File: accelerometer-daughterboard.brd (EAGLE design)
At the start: 3.7 x 11.9 mm, 4 parts, among them U1 LIS3DHTR

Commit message: Tweak
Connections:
- net INT1: now also U$1.P$4
- net SAO: no longer U$1.P$4
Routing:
- net SAO: track 1.59 -> 0.00 mm, vias 1 -> 0
- net INT1: track 0.00 -> 1.57 mm, vias 0 -> 1
- net 3.3V: track 15.7 -> 16.6 mm
- net GND: track 12.9 -> 13.4 mm
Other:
- board text added: "INT1"
- board text removed: "SAO"
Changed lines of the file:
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@@
 <wire x1="9.555834375" y1="16.78234375" x2="8.539834375" y2="17.79834375" width="0.254" layer="21" curve="-90"/>
 <wire x1="8.539834375" y1="17.79834375" x2="9.555834375" y2="18.81434375" width="0.254" layer="21" curve="-92"/>
-<text x="8.81850625" y="13.959309375" size="1.016" layer="22" font="vector" ratio="14" rot="MR0" align="center">SAO</text>
+<text x="8.81850625" y="13.959309375" size="1.016" layer="22" font="vector" ratio="14" rot="MR0" align="center">INT1</text>
 <dimension x1="10.760978125" y1="21.208690625" x2="10.75999375" y2="9.27154375" x3="13.9503125" y3="15.239853125" textsize="1.778" layer="47"/>
 <dimension x1="7.021409375" y1="9.268590625" x2="10.7619625" y2="9.26760625" x3="8.890953125" y3="6.496278125" textsize="1.778" layer="47"/>
@@
 <wire x1="9.1202" y1="12.45" x2="9.1202" y2="12.21" width="0.254" layer="1"/>
 <wire x1="9.1202" y1="12.21" x2="9.4" y2="11.9302" width="0.254" layer="1"/>
-<wire x1="9.0984" y1="12.40656875" x2="8.39" y2="11.69816875" width="0.254" layer="1"/>
 <wire x1="9.1202" y1="12.45" x2="9.0984" y2="12.4282" width="0.254" layer="1"/>
 <wire x1="9.0984" y1="12.4282" x2="9.0984" y2="12.40656875" width="0.254" layer="1"/>
-<wire x1="9.1202" y1="14.05" x2="9.1202" y2="19.71140625" width="0.254" layer="1"/>
-<wire x1="9.1202" y1="19.71140625" x2="9.1202" y2="19.88320625" width="0.254" layer="1"/>
+<wire x1="9.1202" y1="14.05" x2="9.1202" y2="19.88320625" width="0.254" layer="1"/>
 <wire x1="9.14" y1="20.315521875" x2="9.123103125" y2="20.298625" width="0.254" layer="1"/>
 <wire x1="9.123103125" y1="20.298625" x2="9.123103125" y2="19.902309375" width="0.254" layer="1"/>
-<wire x1="8.39" y1="11.69816875" x2="8.39" y2="11.35" width="0.254" layer="1"/>
 <wire x1="9.4" y1="11.9302" x2="9.4" y2="11.36" width="0.254" layer="1"/>
 <wire x1="9.4" y1="11.36" x2="9.39" y2="11.35" width="0.254" layer="1"/>
@@
 <wire x1="8.12900625" y1="13.46588125" x2="7.88815625" y2="13.70673125" width="0.254" layer="1"/>
 <wire x1="8.12900625" y1="13.46588125" x2="9.1202" y2="13.46588125" width="0.254" layer="1"/>
-<wire x1="8.89244375" y1="13.46588125" x2="9.1202" y2="13.46588125" width="0" layer="19" extent="1-16"/>
-<wire x1="9.1202" y1="19.71140625" x2="9.123103125" y2="19.902309375" width="0" layer="19" extent="1-1"/>
-<wire x1="8.89244375" y1="13.46588125" x2="9.39" y2="14.05" width="0" layer="19" extent="1-1"/>
-<wire x1="9.1202" y1="19.71140625" x2="9.1202" y2="19.71140625" width="0.254" layer="1"/>
+<wire x1="8.39" y1="11.35" x2="8.39" y2="11.007790625" width="0.254" layer="1"/>
+<wire x1="8.39" y1="11.007790625" x2="8.571953125" y2="10.8258375" width="0.254" layer="1"/>
+<wire x1="9.39" y1="11.35" x2="9.39" y2="11.003521875" width="0.254" layer="1"/>
+<wire x1="9.39" y1="11.003521875" x2="9.139209375" y2="10.75273125" width="0.254" layer="1"/>
+<wire x1="8.571953125" y1="10.8258375" x2="8.645059375" y2="10.75273125" width="0.254" layer="1"/>
+<wire x1="8.645059375" y1="10.75273125" x2="9.139209375" y2="10.75273125" width="0.254" layer="1"/>
 </signal>
 <signal name="SCL_3V">
@@
 <contactref element="U1" pad="14"/>
 <contactref element="U1" pad="1"/>
-<via x="8.874" y="10.19" extent="1-16" drill="0.35"/>
+<via x="8.2553375" y="10.158015625" extent="1-16" drill="0.35"/>
 <wire x1="10.24" y1="12.2" x2="9.844" y2="12.2" width="0.3048" layer="1"/>
 <wire x1="9.844" y1="12.2" x2="9.625" y2="12.419" width="0.3048" layer="1"/>
@@
 <wire x1="7.54" y1="11.87789375" x2="7.4094" y2="11.74729375" width="0.254" layer="1"/>
 <wire x1="7.4094" y1="11.74729375" x2="7.4094" y2="10.95270625" width="0.254" layer="1"/>
-<wire x1="7.4094" y1="10.95270625" x2="7.61770625" y2="10.7444" width="0.254" layer="1"/>
-<wire x1="7.61770625" y1="10.7444" x2="8.3196" y2="10.7444" width="0.3048" layer="1"/>
-<wire x1="8.874" y1="10.19" x2="8.3196" y2="10.7444" width="0.3048" layer="1"/>
+<wire x1="7.4094" y1="10.95270625" x2="8.1756625" y2="10.18644375" width="0.254" layer="1"/>
+<wire x1="8.2553375" y1="10.158015625" x2="8.226909375" y2="10.18644375" width="0.3048" layer="1"/>
+<wire x1="8.226909375" y1="10.18644375" x2="8.1756625" y2="10.18644375" width="0.3048" layer="1"/>
 <wire x1="10.24" y1="12.2" x2="10.24" y2="11.87789375" width="0.3048" layer="1"/>
 <wire x1="10.24" y1="11.87789375" x2="10.3706" y2="11.74729375" width="0.254" layer="1"/>
 <wire x1="10.3706" y1="11.74729375" x2="10.3706" y2="10.9206" width="0.254" layer="1"/>
-<wire x1="10.149875" y1="10.699875" x2="10.225" y2="10.775" width="0.254" layer="1"/>
+<wire x1="9.63685625" y1="10.18685625" x2="10.225" y2="10.775" width="0.254" layer="1"/>
 <wire x1="10.225" y1="10.775" x2="10.3706" y2="10.9206" width="0.254" layer="1"/>
-<wire x1="8.874" y1="10.19" x2="9.383875" y2="10.699875" width="0.3048" layer="1"/>
-<wire x1="9.383875" y1="10.699875" x2="10.149875" y2="10.699875" width="0.3048" layer="1"/>
-<wire x1="10.16229375" y1="10.7444" x2="10.19289375" y2="10.775" width="0.3048" layer="1"/>
+<wire x1="8.2553375" y1="10.158015625" x2="8.284178125" y2="10.18685625" width="0.3048" layer="1"/>
+<wire x1="9.63685625" y1="10.18685625" x2="8.284178125" y2="10.18685625" width="0.3048" layer="1"/>
+<wire x1="9.60059375" y1="10.1827" x2="10.19289375" y2="10.775" width="0.3048" layer="1"/>
 <wire x1="10.19289375" y1="10.775" x2="10.225" y2="10.775" width="0.3048" layer="1"/>
-<wire x1="8.3196" y1="10.7444" x2="10.16229375" y2="10.7444" width="0.3048" layer="1"/>
-<wire x1="8.89" y1="10.16" x2="8.874" y2="10.176" width="0.4064" layer="16"/>
-<wire x1="8.874" y1="10.176" x2="8.874" y2="10.19" width="0.4064" layer="16"/>
+<wire x1="8.2553375" y1="10.158015625" x2="8.280021875" y2="10.1827" width="0.3048" layer="1"/>
+<wire x1="9.60059375" y1="10.1827" x2="8.280021875" y2="10.1827" width="0.3048" layer="1"/>
+<wire x1="8.89" y1="10.16" x2="8.888015625" y2="10.158015625" width="0.4064" layer="16"/>
+<wire x1="8.888015625" y1="10.158015625" x2="8.2553375" y2="10.158015625" width="0.4064" layer="16"/>
 </signal>
 <signal name="INT1">
 <contactref element="U1" pad="11"/>
+<contactref element="U$1" pad="P$4"/>
+<via x="8.3741375" y="12.7071" extent="1-16" drill="0.35"/>
+<wire x1="8.89" y1="11.35" x2="8.88504375" y2="11.35495625" width="0.254" layer="1"/>
+<wire x1="8.3741375" y1="12.2078375" x2="8.3741375" y2="12.7071" width="0.254" layer="1"/>
+<wire x1="8.88504375" y1="11.35495625" x2="8.88504375" y2="11.69693125" width="0.254" layer="1"/>
+<wire x1="8.88504375" y1="11.69693125" x2="8.3741375" y2="12.2078375" width="0.254" layer="1"/>
+<wire x1="8.3741375" y1="12.7071" x2="8.89" y2="12.7" width="0" layer="19" extent="16-16"/>
 </signal>
 <signal name="SAO">
 <contactref element="U1" pad="7"/>
-<contactref element="U$1" pad="P$4"/>
-<via x="8.39" y="12.7" extent="1-16" drill="0.35"/>
-<wire x1="7.54" y1="12.7" x2="8" y2="12.7" width="0.254" layer="1"/>
-<wire x1="8" y1="12.7" x2="8.24341875" y2="12.7" width="0.254" layer="1"/>
-<wire x1="8.39" y1="12.7" x2="8" y2="12.7" width="0.254" layer="1"/>
-<wire x1="8.89" y1="12.7" x2="8.39" y2="12.7" width="0.4064" layer="16"/>
 </signal>
 <signal name="ADC1">

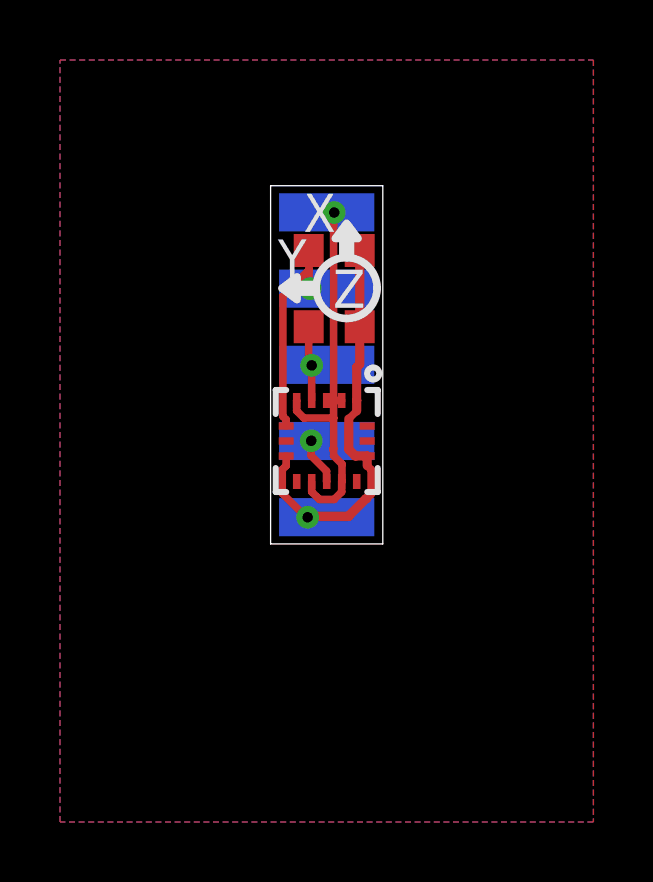
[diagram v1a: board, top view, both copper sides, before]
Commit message: Re-add buffer caps
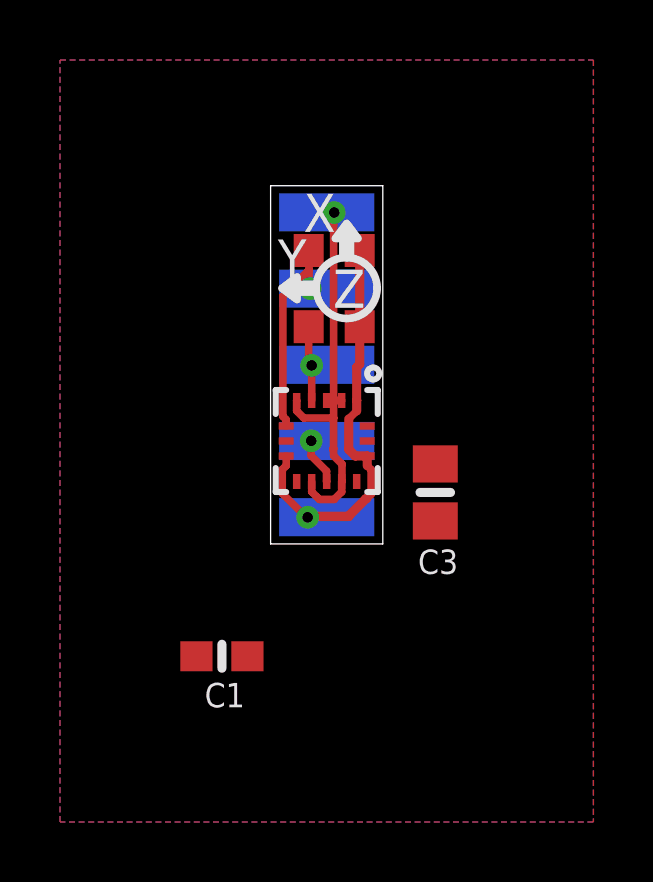
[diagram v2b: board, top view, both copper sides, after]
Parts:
- added C1: 0.1uF, microbuilder:0603-NO
- added C3: 10uF, microbuilder:0805-NO
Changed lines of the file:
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@@
 </autorouter>
 <elements>
+<element name="C3" library="microbuilder" package="0805-NO" value="10uF" x="12.5095" y="10.9855" smashed="yes" rot="R270">
+<attribute name="NAME" x="13.2715" y="9.0805" size="0.8128" layer="25" ratio="18" rot="R180"/>
+<attribute name="VALUE" x="11.557" y="10.033" size="1.016" layer="27" ratio="10" rot="R90"/>
+</element>
+<element name="C1" library="microbuilder" package="0603-NO" value="0.1uF" x="5.3975" y="5.5245" smashed="yes" rot="R180">
+<attribute name="NAME" x="6.1595" y="4.6355" size="0.8128" layer="25" ratio="18" rot="R180"/>
+<attribute name="VALUE" x="3.937" y="5.1435" size="1.016" layer="27" ratio="10" rot="R180"/>
+</element>
 <element name="U1" library="microbuilder" package="LGA16_3X3MM" value="LIS3DHTR" x="8.89" y="12.7" smashed="yes" rot="R270">
 <attribute name="VALUE" x="7.952" y="14.4275" size="1.016" layer="27" ratio="12"/>

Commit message: remove caps again
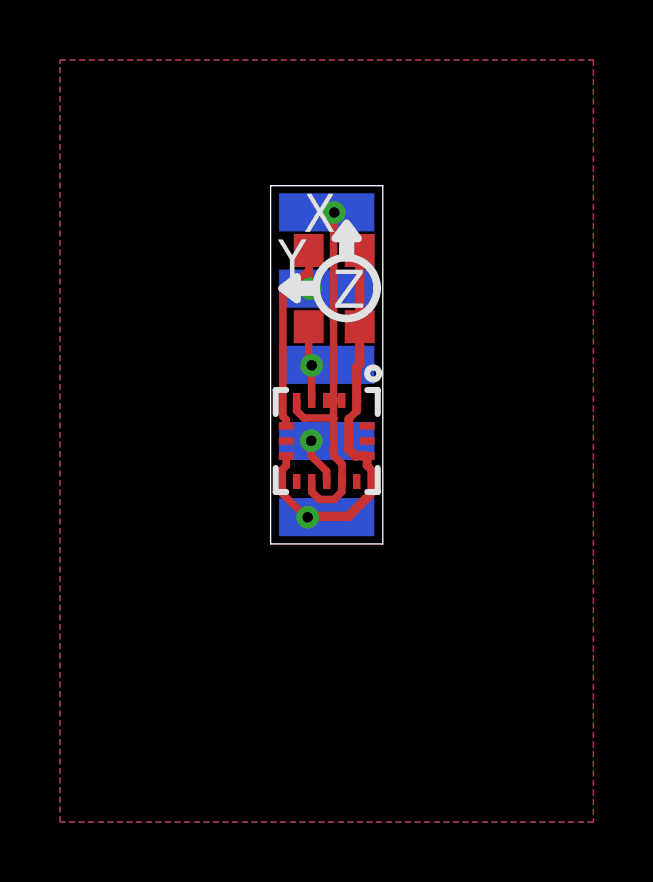
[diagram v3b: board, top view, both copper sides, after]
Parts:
- removed C1: 0.1uF, microbuilder:0603-NO
- removed C3: 10uF, microbuilder:0805-NO
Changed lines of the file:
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@@
 </autorouter>
 <elements>
-<element name="C3" library="microbuilder" package="0805-NO" value="10uF" x="12.5095" y="10.9855" smashed="yes" rot="R270">
-<attribute name="NAME" x="13.2715" y="9.0805" size="0.8128" layer="25" ratio="18" rot="R180"/>
-<attribute name="VALUE" x="11.557" y="10.033" size="1.016" layer="27" ratio="10" rot="R90"/>
-</element>
-<element name="C1" library="microbuilder" package="0603-NO" value="0.1uF" x="5.3975" y="5.5245" smashed="yes" rot="R180">
-<attribute name="NAME" x="6.1595" y="4.6355" size="0.8128" layer="25" ratio="18" rot="R180"/>
-<attribute name="VALUE" x="3.937" y="5.1435" size="1.016" layer="27" ratio="10" rot="R180"/>
-</element>
 <element name="U1" library="microbuilder" package="LGA16_3X3MM" value="LIS3DHTR" x="8.89" y="12.7" smashed="yes" rot="R270">
 <attribute name="VALUE" x="7.952" y="14.4275" size="1.016" layer="27" ratio="12"/>
@@
 <wire x1="8.12900625" y1="13.46588125" x2="9.1202" y2="13.46588125" width="0.254" layer="1"/>
 <wire x1="8.39" y1="11.35" x2="8.39" y2="11.007790625" width="0.254" layer="1"/>
-<wire x1="8.39" y1="11.007790625" x2="8.571953125" y2="10.8258375" width="0.254" layer="1"/>
+<wire x1="8.39" y1="11.007790625" x2="8.645059375" y2="10.75273125" width="0.254" layer="1"/>
 <wire x1="9.39" y1="11.35" x2="9.39" y2="11.003521875" width="0.254" layer="1"/>
 <wire x1="9.39" y1="11.003521875" x2="9.139209375" y2="10.75273125" width="0.254" layer="1"/>
-<wire x1="8.571953125" y1="10.8258375" x2="8.645059375" y2="10.75273125" width="0.254" layer="1"/>
 <wire x1="8.645059375" y1="10.75273125" x2="9.139209375" y2="10.75273125" width="0.254" layer="1"/>
+<wire x1="9.1202" y1="19.88320625" x2="9.123103125" y2="19.902309375" width="0" layer="19" extent="1-1"/>
+<wire x1="9.1" y1="14.05" x2="9.39" y2="14.05" width="0" layer="19" extent="1-1"/>
 </signal>
 <signal name="SCL_3V">
